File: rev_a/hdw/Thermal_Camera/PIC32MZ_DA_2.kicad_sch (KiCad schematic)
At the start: 0 parts

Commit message: finished PIC32MZ DA symbol
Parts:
- added U?: PIC32MZ2064DAR176, Custom Footprints Library:LQFP-176_20x20mm_P0.4mm_7p9x7p9mm_EP, symbol Custom Library:PIC32MZ2064DAR176
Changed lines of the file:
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@@
     (company "Drew Maatman and Michael Laffin")
   )
+  (symbol (lib_id "Custom Library:PIC32MZ2064DAR176") (at 135.89 85.09 0) (unit 3)
+    (in_bom yes) (on_board yes) (dnp no)
+    (property "Reference" "U?" (at 100.33 35.56 0)
+      (effects (font (size 1.27 1.27)) (justify left))
+    )
+    (property "Value" "PIC32MZ2064DAR176" (at 100.33 38.1 0)
+      (effects (font (size 1.27 1.27)) (justify left))
+    )
+    (property "Footprint" "Custom Footprints Library:LQFP-176_20x20mm_P0.4mm_7p9x7p9mm_EP" (at 100.33 40.64 0)
+      (effects (font (size 1.27 1.27)) (justify left) hide)
+    )
+    (property "Datasheet" "https://ww1.microchip.com/downloads/aemDocuments/documents/MCU32/ProductDocuments/DataSheets/PIC32MZ-Graphics-%28DAK-DAL-DAR-DAS%29-Family-Datasheet-DS60001565D.pdf" (at 100.33 45.72 0)
+      (effects (font (size 1.27 1.27)) (justify left) hide)
+    )
+    (property "Digi-Key PN" "PIC32MZ2064DAR176-I/2J-ND" (at 135.89 85.09 0)
+      (effects (font (size 1.27 1.27)) hide)
+    )
+    (pin "23")
+    (pin "77")
+    (pin "79")
+    (pin "111")
+    (pin "54")
+    (pin "118")
+    (pin "132")
+    (pin "146")
+    (pin "148")
+    (pin "24")
+    (pin "75")
+    (pin "140")
+    (pin "144")
+    (pin "152")
+    (pin "53")
+    (pin "108")
+    (pin "69")
+    (pin "101")
+    (pin "130")
+    (pin "100")
+    (pin "135")
+    (pin "137")
+    (pin "71")
+    (pin "105")
+    (pin "9")
+    (pin "133")
+    (pin "138")
+    (pin "55")
+    (pin "98")
+    (pin "2")
+    (pin "80")
+    (pin "99")
+    (pin "81")
+    (pin "7")
+    (pin "74")
+    (pin "104")
+    (pin "106")
+    (pin "8")
+    (pin "73")
+    (pin "109")
+    (pin "113")
+    (pin "76")
+    (pin "25")
+    (pin "70")
+    (pin "107")
+    (pin "134")
+    (pin "139")
+    (pin "26")
+    (pin "114")
+    (pin "141")
+    (pin "143")
+    (pin "142")
+    (pin "149")
+    (pin "150")
+    (pin "136")
+    (pin "151")
+    (pin "147")
+    (pin "36")
+    (pin "110")
+    (pin "40")
+    (pin "145")
+    (pin "112")
+    (pin "131")
+    (pin "43")
+    (pin "93")
+    (pin "27")
+    (pin "89")
+    (pin "97")
+    (pin "35")
+    (pin "32")
+    (pin "41")
+    (pin "42")
+    (pin "56")
+    (pin "65")
+    (pin "90")
+    (pin "91")
+    (pin "95")
+    (pin "31")
+    (pin "28")
+    (pin "96")
+    (pin "34")
+    (pin "82")
+    (pin "64")
+    (pin "30")
+    (pin "92")
+    (pin "33")
+    (pin "86")
+    (pin "88")
+    (pin "44")
+    (pin "115")
+    (pin "50")
+    (pin "155")
+    (pin "59")
+    (pin "66")
+    (pin "78")
+    (pin "83")
+    (pin "63")
+    (pin "84")
+    (pin "153")
+    (pin "18")
+    (pin "51")
+    (pin "39")
+    (pin "46")
+    (pin "87")
+    (pin "37")
+    (pin "72")
+    (pin "176")
+    (pin "85")
+    (pin "4")
+    (pin "20")
+    (pin "48")
+    (pin "58")
+    (pin "94")
+    (pin "11")
+    (pin "119")
+    (pin "102")
+    (pin "22")
+    (pin "166")
+    (pin "3")
+    (pin "21")
+    (pin "38")
+    (pin "60")
+    (pin "62")
+    (pin "68")
+    (pin "52")
+    (pin "10")
+    (pin "117")
+    (pin "29")
+    (pin "165")
+    (pin "6")
+    (pin "1")
+    (pin "49")
+    (pin "124")
+    (pin "123")
+    (pin "122")
+    (pin "120")
+    (pin "156")
+    (pin "12")
+    (pin "5")
+    (pin "121")
+    (pin "177")
+    (pin "19")
+    (pin "47")
+    (pin "45")
+    (pin "103")
+    (pin "57")
+    (pin "61")
+    (pin "116")
+    (pin "154")
+    (pin "67")
+    (pin "17")
+    (pin "159")
+    (pin "126")
+    (pin "168")
+    (pin "170")
+    (pin "158")
+    (pin "160")
+    (pin "172")
+    (pin "173")
+    (pin "163")
+    (pin "174")
+    (pin "16")
+    (pin "175")
+    (pin "161")
+    (pin "167")
+    (pin "128")
+    (pin "164")
+    (pin "129")
+    (pin "162")
+    (pin "125")
+    (pin "127")
+    (pin "13")
+    (pin "168")
+    (pin "171")
+    (pin "14")
+    (pin "15")
+    (pin "157")
+    (instances
+      (project "Thermal_Camera"
+        (path "/4bd21e0b-5408-4b93-866e-c82ac5b31fa9/d6dd27c9-8e5b-4d17-a34a-73b51937c448"
+          (reference "U?") (unit 3)
+        )
+      )
+    )
+  )
 )

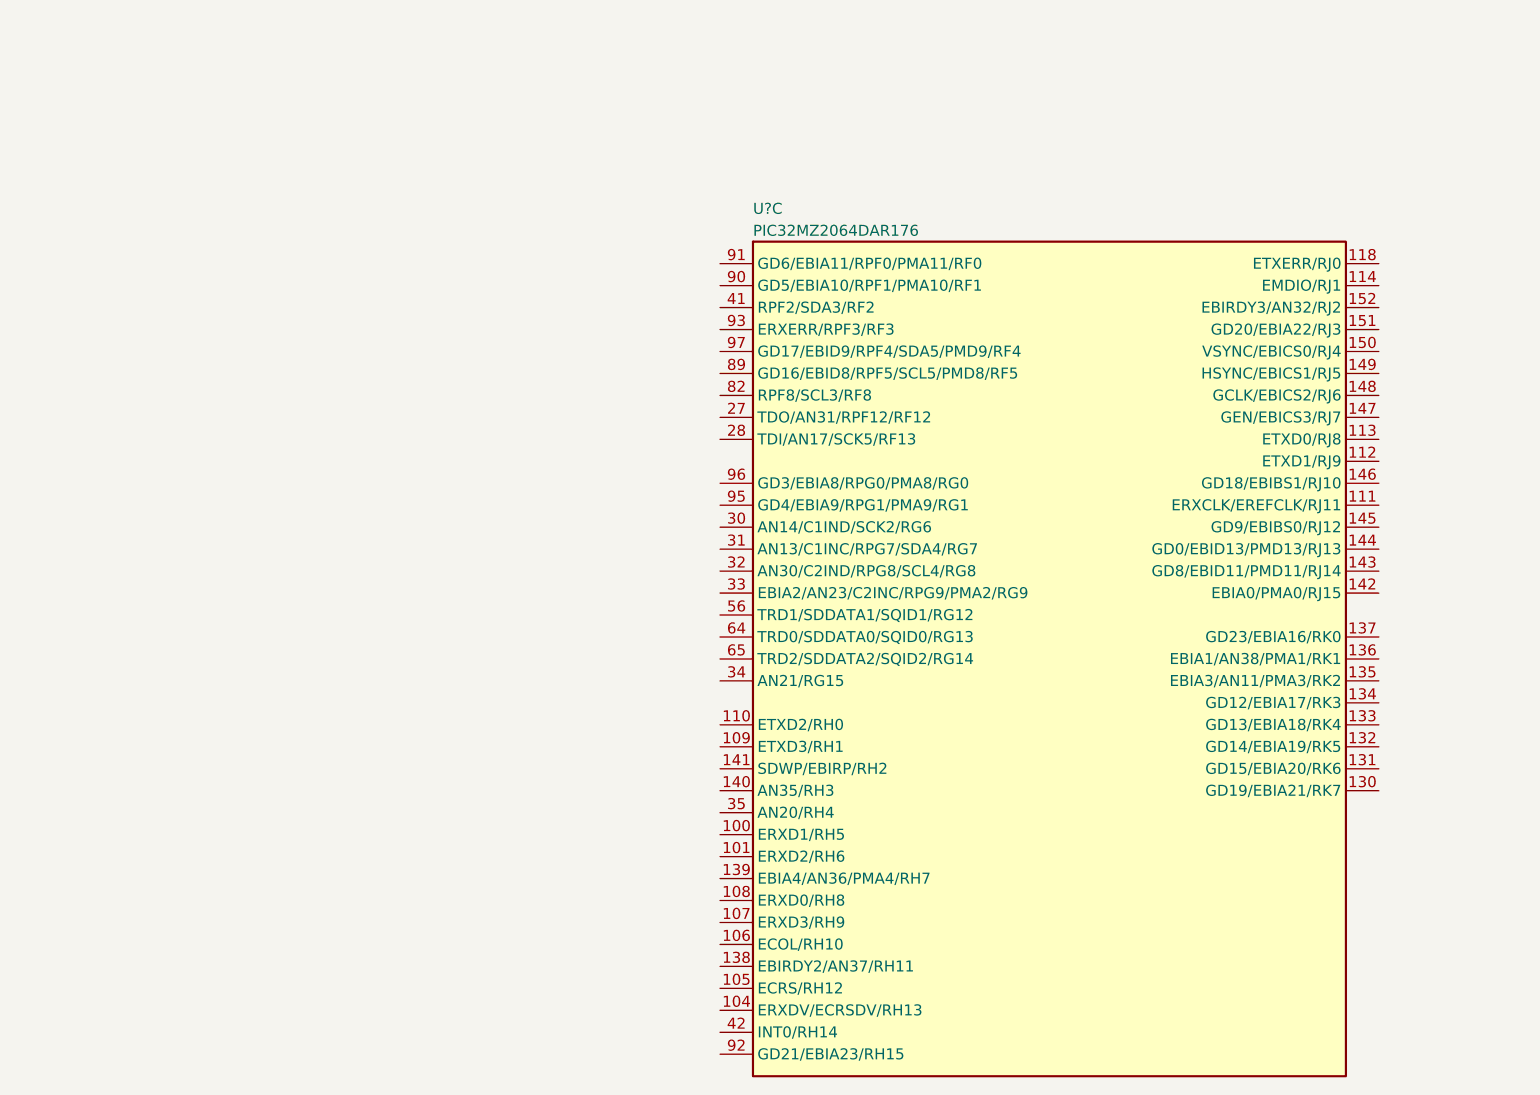
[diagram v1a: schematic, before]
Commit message: added lepton sensor, made some other schematic progress
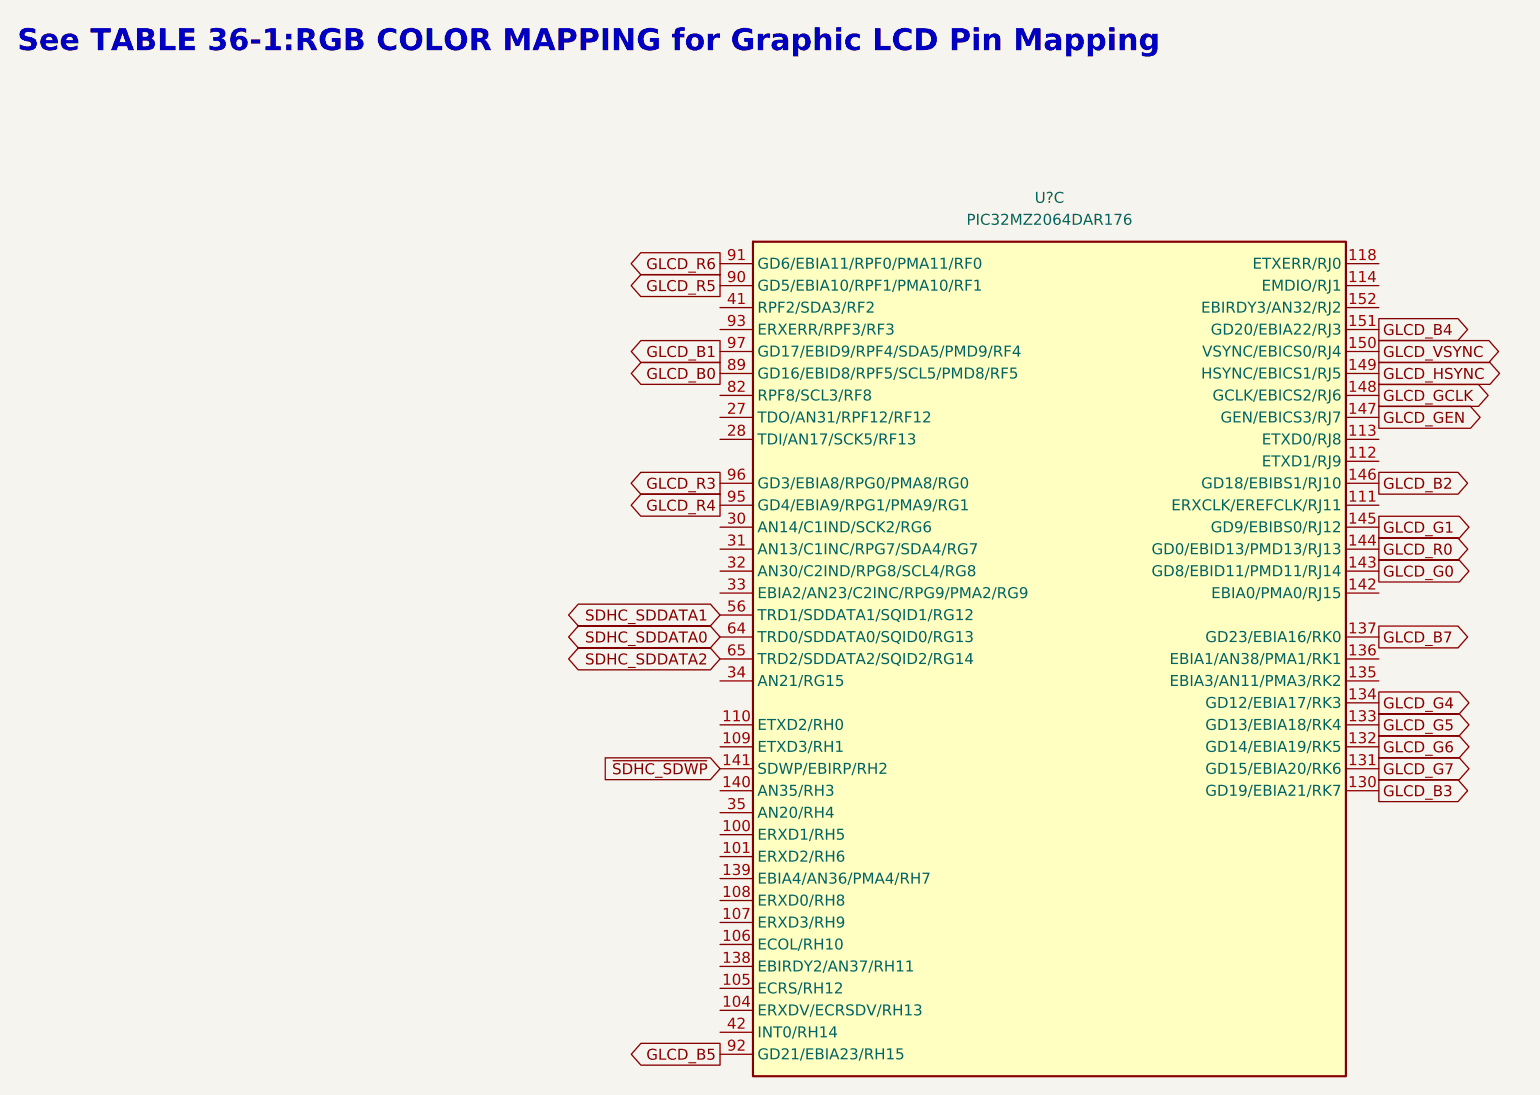
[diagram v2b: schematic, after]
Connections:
- net GLCD_B3: now reaches U?.130 (GD19/EBIA21/RK7)
- net GLCD_G7: now reaches U?.131 (GD15/EBIA20/RK6)
- net GLCD_G6: now reaches U?.132 (GD14/EBIA19/RK5)
- net GLCD_G5: now reaches U?.133 (GD13/EBIA18/RK4)
- net GLCD_G4: now reaches U?.134 (GD12/EBIA17/RK3)
- net GLCD_B7: now reaches U?.137 (GD23/EBIA16/RK0)
- net ~{SDHC_SDWP}: now reaches U?.141 (SDWP/EBIRP/RH2)
- net GLCD_G0: now reaches U?.143 (GD8/EBID11/PMD11/RJ14)
- net GLCD_R0: now reaches U?.144 (GD0/EBID13/PMD13/RJ13)
- net GLCD_G1: now reaches U?.145 (GD9/EBIBS0/RJ12)
- net GLCD_B2: now reaches U?.146 (GD18/EBIBS1/RJ10)
- net GLCD_GEN: now reaches U?.147 (GEN/EBICS3/RJ7)
- net GLCD_GCLK: now reaches U?.148 (GCLK/EBICS2/RJ6)
- net GLCD_HSYNC: now reaches U?.149 (HSYNC/EBICS1/RJ5)
- net GLCD_VSYNC: now reaches U?.150 (VSYNC/EBICS0/RJ4)
- net GLCD_B4: now reaches U?.151 (GD20/EBIA22/RJ3)
- net SDHC_SDDATA1: now reaches U?.56 (TRD1/SDDATA1/SQID1/RG12)
- net SDHC_SDDATA0: now reaches U?.64 (TRD0/SDDATA0/SQID0/RG13)
- net SDHC_SDDATA2: now reaches U?.65 (TRD2/SDDATA2/SQID2/RG14)
- net GLCD_B0: now reaches U?.89 (GD16/EBID8/RPF5/SCL5/PMD8/RF5)
- net GLCD_R5: now reaches U?.90 (GD5/EBIA10/RPF1/PMA10/RF1)
- net GLCD_R6: now reaches U?.91 (GD6/EBIA11/RPF0/PMA11/RF0)
- net GLCD_B5: now reaches U?.92 (GD21/EBIA23/RH15)
- net GLCD_R4: now reaches U?.95 (GD4/EBIA9/RPG1/PMA9/RG1)
- net GLCD_R3: now reaches U?.96 (GD3/EBIA8/RPG0/PMA8/RG0)
- net GLCD_B1: now reaches U?.97 (GD17/EBID9/RPF4/SDA5/PMD9/RF4)
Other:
- note added: "See TABLE 36-1:RGB COLOR MAPPING for Graphic LCD Pin Mapping"
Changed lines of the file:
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@@
   (title_block
     (title "Thermal Camera")
-    (date "2023-11-11")
+    (date "2023-11-12")
     (rev "PRELIM")
     (company "Drew Maatman and Michael Laffin")
   )
+  (text "See TABLE 36-1:RGB COLOR MAPPING for Graphic LCD Pin Mapping"
+    (at 15.24 17.78 0)
+    (effects (font (face "Courier New") (size 2.54 2.54) (thickness 0.254) bold) (justify left bottom))
+  )
+  (global_label "GLCD_R4" (shape output) (at 96.52 69.85 180) (fields_autoplaced)
+    (effects (font (size 1.27 1.27)) (justify right))
+    (property "Intersheetrefs" "${INTERSHEET_REFS}" (at 85.2496 69.85 0)
+      (effects (font (size 1.27 1.27)) (justify right) hide)
+    )
+  )
+  (global_label "GLCD_R5" (shape output) (at 96.52 44.45 180) (fields_autoplaced)
+    (effects (font (size 1.27 1.27)) (justify right))
+    (property "Intersheetrefs" "${INTERSHEET_REFS}" (at 85.2496 44.45 0)
+      (effects (font (size 1.27 1.27)) (justify right) hide)
+    )
+  )
+  (global_label "GLCD_B1" (shape output) (at 96.52 52.07 180) (fields_autoplaced)
+    (effects (font (size 1.27 1.27)) (justify right))
+    (property "Intersheetrefs" "${INTERSHEET_REFS}" (at 85.2496 52.07 0)
+      (effects (font (size 1.27 1.27)) (justify right) hide)
+    )
+  )
+  (global_label "GLCD_G1" (shape output) (at 172.72 72.39 0) (fields_autoplaced)
+    (effects (font (size 1.27 1.27)) (justify left))
+    (property "Intersheetrefs" "${INTERSHEET_REFS}" (at 183.9904 72.39 0)
+      (effects (font (size 1.27 1.27)) (justify left) hide)
+    )
+  )
+  (global_label "SDHC_SDDATA1" (shape bidirectional) (at 96.52 82.55 180) (fields_autoplaced)
+    (effects (font (size 1.27 1.27)) (justify right))
+    (property "Intersheetrefs" "${INTERSHEET_REFS}" (at 78.2721 82.55 0)
+      (effects (font (size 1.27 1.27)) (justify right) hide)
+    )
+  )
+  (global_label "GLCD_HSYNC" (shape output) (at 172.72 54.61 0) (fields_autoplaced)
+    (effects (font (size 1.27 1.27)) (justify left))
+    (property "Intersheetrefs" "${INTERSHEET_REFS}" (at 187.74 54.61 0)
+      (effects (font (size 1.27 1.27)) (justify left) hide)
+    )
+  )
+  (global_label "GLCD_G6" (shape output) (at 172.72 97.79 0) (fields_autoplaced)
+    (effects (font (size 1.27 1.27)) (justify left))
+    (property "Intersheetrefs" "${INTERSHEET_REFS}" (at 183.9904 97.79 0)
+      (effects (font (size 1.27 1.27)) (justify left) hide)
+    )
+  )
+  (global_label "GLCD_R3" (shape output) (at 96.52 67.31 180) (fields_autoplaced)
+    (effects (font (size 1.27 1.27)) (justify right))
+    (property "Intersheetrefs" "${INTERSHEET_REFS}" (at 85.2496 67.31 0)
+      (effects (font (size 1.27 1.27)) (justify right) hide)
+    )
+  )
+  (global_label "GLCD_G0" (shape output) (at 172.72 77.47 0) (fields_autoplaced)
+    (effects (font (size 1.27 1.27)) (justify left))
+    (property "Intersheetrefs" "${INTERSHEET_REFS}" (at 183.9904 77.47 0)
+      (effects (font (size 1.27 1.27)) (justify left) hide)
+    )
+  )
+  (global_label "GLCD_R6" (shape output) (at 96.52 41.91 180) (fields_autoplaced)
+    (effects (font (size 1.27 1.27)) (justify right))
+    (property "Intersheetrefs" "${INTERSHEET_REFS}" (at 85.2496 41.91 0)
+      (effects (font (size 1.27 1.27)) (justify right) hide)
+    )
+  )
+  (global_label "GLCD_B2" (shape output) (at 172.72 67.31 0) (fields_autoplaced)
+    (effects (font (size 1.27 1.27)) (justify left))
+    (property "Intersheetrefs" "${INTERSHEET_REFS}" (at 183.9904 67.31 0)
+      (effects (font (size 1.27 1.27)) (justify left) hide)
+    )
+  )
+  (global_label "GLCD_B3" (shape output) (at 172.72 102.87 0) (fields_autoplaced)
+    (effects (font (size 1.27 1.27)) (justify left))
+    (property "Intersheetrefs" "${INTERSHEET_REFS}" (at 183.9904 102.87 0)
+      (effects (font (size 1.27 1.27)) (justify left) hide)
+    )
+  )
+  (global_label "GLCD_GEN" (shape output) (at 172.72 59.69 0) (fields_autoplaced)
+    (effects (font (size 1.27 1.27)) (justify left))
+    (property "Intersheetrefs" "${INTERSHEET_REFS}" (at 185.2604 59.69 0)
+      (effects (font (size 1.27 1.27)) (justify left) hide)
+    )
+  )
+  (global_label "GLCD_VSYNC" (shape output) (at 172.72 52.07 0) (fields_autoplaced)
+    (effects (font (size 1.27 1.27)) (justify left))
+    (property "Intersheetrefs" "${INTERSHEET_REFS}" (at 187.4981 52.07 0)
+      (effects (font (size 1.27 1.27)) (justify left) hide)
+    )
+  )
+  (global_label "GLCD_B7" (shape output) (at 172.72 85.09 0) (fields_autoplaced)
+    (effects (font (size 1.27 1.27)) (justify left))
+    (property "Intersheetrefs" "${INTERSHEET_REFS}" (at 183.9904 85.09 0)
+      (effects (font (size 1.27 1.27)) (justify left) hide)
+    )
+  )
+  (global_label "GLCD_G4" (shape output) (at 172.72 92.71 0) (fields_autoplaced)
+    (effects (font (size 1.27 1.27)) (justify left))
+    (property "Intersheetrefs" "${INTERSHEET_REFS}" (at 183.9904 92.71 0)
+      (effects (font (size 1.27 1.27)) (justify left) hide)
+    )
+  )
+  (global_label "SDHC_SDDATA0" (shape bidirectional) (at 96.52 85.09 180) (fields_autoplaced)
+    (effects (font (size 1.27 1.27)) (justify right))
+    (property "Intersheetrefs" "${INTERSHEET_REFS}" (at 78.2721 85.09 0)
+      (effects (font (size 1.27 1.27)) (justify right) hide)
+    )
+  )
+  (global_label "GLCD_B4" (shape output) (at 172.72 49.53 0) (fields_autoplaced)
+    (effects (font (size 1.27 1.27)) (justify left))
+    (property "Intersheetrefs" "${INTERSHEET_REFS}" (at 183.9904 49.53 0)
+      (effects (font (size 1.27 1.27)) (justify left) hide)
+    )
+  )
+  (global_label "GLCD_B5" (shape output) (at 96.52 133.35 180) (fields_autoplaced)
+    (effects (font (size 1.27 1.27)) (justify right))
+    (property "Intersheetrefs" "${INTERSHEET_REFS}" (at 85.2496 133.35 0)
+      (effects (font (size 1.27 1.27)) (justify right) hide)
+    )
+  )
+  (global_label "SDHC_SDDATA2" (shape bidirectional) (at 96.52 87.63 180) (fields_autoplaced)
+    (effects (font (size 1.27 1.27)) (justify right))
+    (property "Intersheetrefs" "${INTERSHEET_REFS}" (at 78.2721 87.63 0)
+      (effects (font (size 1.27 1.27)) (justify right) hide)
+    )
+  )
+  (global_label "GLCD_B0" (shape output) (at 96.52 54.61 180) (fields_autoplaced)
+    (effects (font (size 1.27 1.27)) (justify right))
+    (property "Intersheetrefs" "${INTERSHEET_REFS}" (at 85.2496 54.61 0)
+      (effects (font (size 1.27 1.27)) (justify right) hide)
+    )
+  )
+  (global_label "~{SDHC_SDWP}" (shape input) (at 96.52 100.33 180) (fields_autoplaced)
+    (effects (font (size 1.27 1.27)) (justify right))
+    (property "Intersheetrefs" "${INTERSHEET_REFS}" (at 82.2863 100.33 0)
+      (effects (font (size 1.27 1.27)) (justify right) hide)
+    )
+  )
+  (global_label "GLCD_R0" (shape output) (at 172.72 74.93 0) (fields_autoplaced)
+    (effects (font (size 1.27 1.27)) (justify left))
+    (property "Intersheetrefs" "${INTERSHEET_REFS}" (at 183.9904 74.93 0)
+      (effects (font (size 1.27 1.27)) (justify left) hide)
+    )
+  )
+  (global_label "GLCD_G5" (shape output) (at 172.72 95.25 0) (fields_autoplaced)
+    (effects (font (size 1.27 1.27)) (justify left))
+    (property "Intersheetrefs" "${INTERSHEET_REFS}" (at 183.9904 95.25 0)
+      (effects (font (size 1.27 1.27)) (justify left) hide)
+    )
+  )
+  (global_label "GLCD_G7" (shape output) (at 172.72 100.33 0) (fields_autoplaced)
+    (effects (font (size 1.27 1.27)) (justify left))
+    (property "Intersheetrefs" "${INTERSHEET_REFS}" (at 183.9904 100.33 0)
+      (effects (font (size 1.27 1.27)) (justify left) hide)
+    )
+  )
+  (global_label "GLCD_GCLK" (shape output) (at 172.72 57.15 0) (fields_autoplaced)
+    (effects (font (size 1.27 1.27)) (justify left))
+    (property "Intersheetrefs" "${INTERSHEET_REFS}" (at 186.349 57.15 0)
+      (effects (font (size 1.27 1.27)) (justify left) hide)
+    )
+  )
   (symbol (lib_id "Custom Library:PIC32MZ2064DAR176") (at 135.89 85.09 0) (unit 3)
-    (in_bom yes) (on_board yes) (dnp no)
-    (property "Reference" "U?" (at 100.33 35.56 0)
-      (effects (font (size 1.27 1.27)) (justify left))
+    (in_bom yes) (on_board yes) (dnp no) (fields_autoplaced)
+    (property "Reference" "U?" (at 134.62 34.29 0)
+      (effects (font (size 1.27 1.27)))
     )
-    (property "Value" "PIC32MZ2064DAR176" (at 100.33 38.1 0)
-      (effects (font (size 1.27 1.27)) (justify left))
+    (property "Value" "PIC32MZ2064DAR176" (at 134.62 36.83 0)
+      (effects (font (size 1.27 1.27)))
     )
     (property "Footprint" "Custom Footprints Library:LQFP-176_20x20mm_P0.4mm_7p9x7p9mm_EP" (at 100.33 40.64 0)
